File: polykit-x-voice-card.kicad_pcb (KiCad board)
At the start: 2 copper layers, 200 x 100 mm, 206 parts, among them J1 Conn_01x36, Q1 2N3904, U1 4016, U10 CD4051B, U2 TL072, U3 4016, U4 TL074, U5 AS3372E, U6 AS3340, U7 AS3310, U8 TL074, U9 TL074

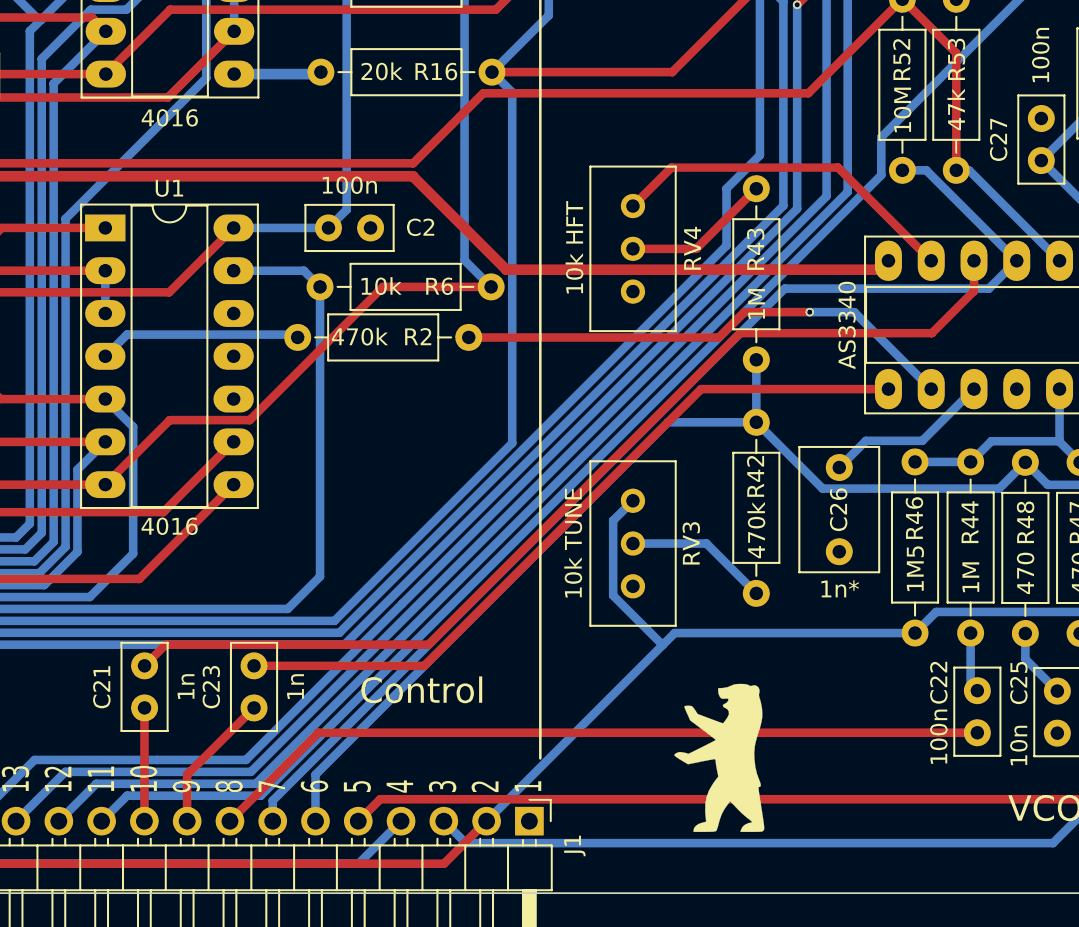
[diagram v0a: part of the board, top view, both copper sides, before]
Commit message: - add R38 offset to IN1 - change 4016 to 4066
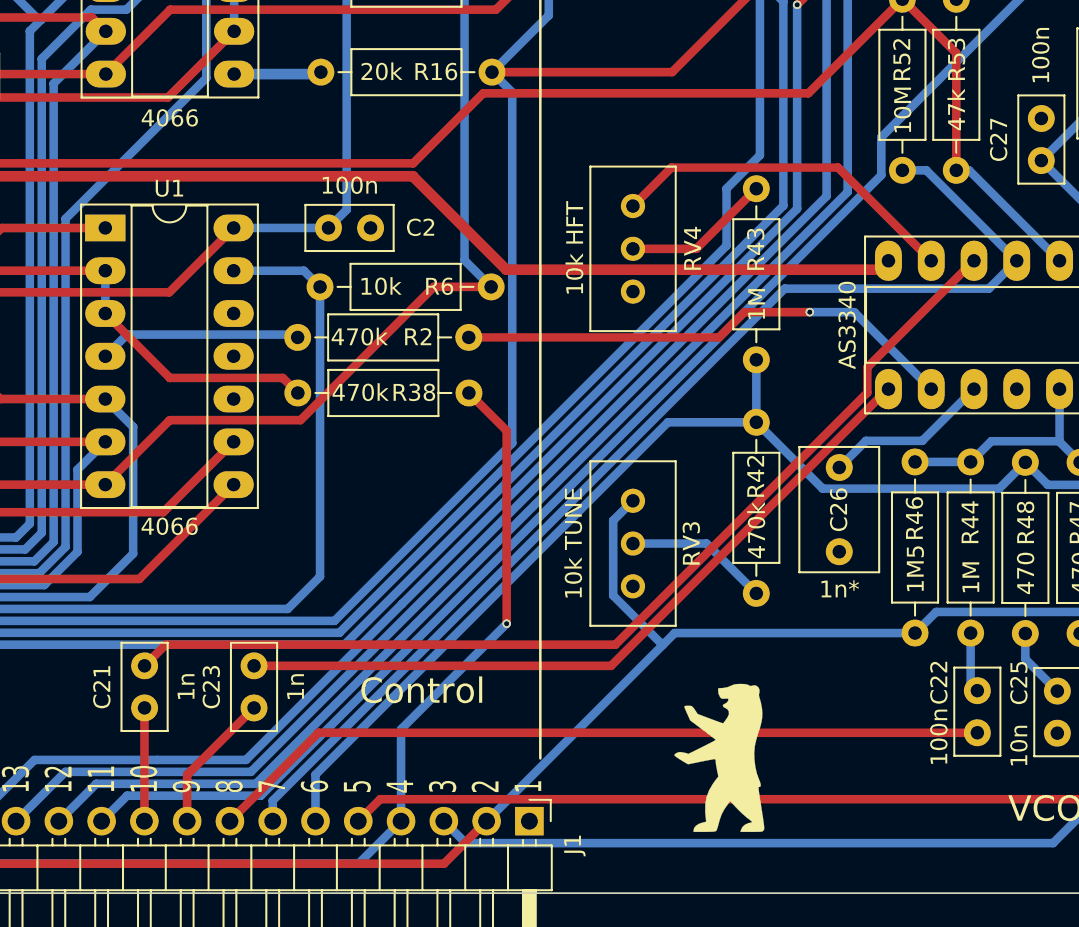
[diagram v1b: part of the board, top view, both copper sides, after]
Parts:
- added R38: 470k, Resistor_THT:R_Axial_DIN0207_L6.3mm_D2.5mm_P10.16mm_Horizontal, F.Cu at (180.6, 105.3)
- U1, U3: value 4016 -> 4066
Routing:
- net +5V: track 174.9 -> 203.9 mm, vias 1 -> 2
- net IN1: track 44.0 -> 57.4 mm
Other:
- board text added: "Polykit-X Voice Card v0.0.4 Jan Knipper 2022 - github.com/polykit"
- board text removed: "Polykit-X Voice Card v0.0.3 Jan Knipper 2022 - github.com/polykit"

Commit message: Bump to v1.0.0
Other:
- board text added: "Polykit-X Voice Card v1.0.0 Jan Knipper 2023 - github.com/polykit"
- board text removed: "Polykit-X Voice Card v0.0.4 Jan Knipper 2022 - github.com/polykit"
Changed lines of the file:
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@@
   (title_block
     (title "Polykit-X Voice Card")
-    (date "2022-08-24")
-    (rev "v0.0.4")
+    (date "2023-01-26")
+    (rev "v1.0.0")
     (company "Jan Knipper")
     (comment 1 "github.com/polykit")
@@
     (effects (font (size 0.8 0.8) (thickness 0.15)) (justify mirror))
   )
-  (gr_text "Polykit-X Voice Card v0.0.4\nJan Knipper 2022 - github.com/polykit" (at 151 38) (layer "B.SilkS")
+  (gr_text "Polykit-X Voice Card v1.0.0\nJan Knipper 2023 - github.com/polykit" (at 151 38) (layer "B.SilkS")
     (effects (font (size 1.5 1.5) (thickness 0.25)) (justify mirror))
   )
